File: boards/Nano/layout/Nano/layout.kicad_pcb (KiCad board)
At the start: 4 copper layers, 22 x 22 mm, 26 parts, among them U1 ?

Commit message: first pass
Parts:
- removed H1, H2, H3, H4: M2 DIN965 TopBottom, MountingHole_2.2mm_M2_DIN965_Pad_TopBottom:MountingHole_2.2mm_M2_DIN965_Pad_TopBottom
- removed R10: 1k, R_0402_1005Metric:R_0402_1005Metric
- removed R6, R7, R8, R9: 820, R_0402_1005Metric:R_0402_1005Metric
- removed U1: ?, InvenSense_QFN-24_3x3mm_P0.4mm:InvenSense_QFN-24_3x3mm_P0.4mm
- added C10: 100nF 10V, C_0402_1005Metric:C_0402_1005Metric, B.Cu at (80.5, 103.9)
- added C11: 100nF 6.3V, C_0402_1005Metric:C_0402_1005Metric, F.Cu at (85.4, 108.7)
- added C12: 100nF 10V, C_0402_1005Metric:C_0402_1005Metric, F.Cu at (83.1, 101.6)
- added C13: 100nF 10V, C_0402_1005Metric:C_0402_1005Metric, F.Cu at (87.6, 103.4)
- added C14: 100nF 10V, C_0402_1005Metric:C_0402_1005Metric, F.Cu at (87.6, 104.3)
- added C15: 4.7uF 10V, C_0603_1608Metric:C_0603_1608Metric, F.Cu at (88.2, 105.6)
- added IC1: ATMEGA328PMAU, QFP80P900X900X120-32N:QFP80P900X900X120-32N, F.Cu at (86.8, 120.3)
- added IC2: AMS1117M5_0, SOT229P700X180-4N:SOT229P700X180-4N, B.Cu at (84.7, 107.2)
- added IC3: FT231XQMR, QFN50P400X400X80-21N:QFN50P400X400X80-21N, F.Cu at (84.0, 105.1)
- added J1: 2.54mm 15x1, PinHeader_1x15_P2.54mm_Vertical:PinHeader_1x15_P2.54mm_Vertical, B.Cu at (75.1, 95.2)
- added J2: 2.54mm 15x1, PinHeader_1x15_P2.54mm_Vertical:PinHeader_1x15_P2.54mm_Vertical, B.Cu at (96.0, 95.2)
- added J3: 10118194M0001LF, 101181940001LF:101181940001LF, F.Cu at (85.3, 92.9)
- added J4: 2.54mm 3x2, PinHeader_2x03_P2.54mm_Vertical:PinHeader_2x03_P2.54mm_Vertical, F.Cu at (82.7, 134.4)
- added S1: SKRKAHE020, SKRKAEE020:SKRKAEE020, F.Cu at (79.3, 116.0)
- added Y1: 16MHz 18pF, Crystal_SMD_3225-4Pin_3.2x2.5mm:Crystal_SMD_3225-4Pin_3.2x2.5mm, F.Cu at (79.4, 123.7)
- C2, C3: value 100nF -> 100nF 6.3V
- C4: value 10nF -> 100nF 6.3V
- C5, C6: value 10nF -> 22pF C0G
- C7: value 10nF -> 10uF 25V; footprint C_0402_1005Metric:C_0402_1005Metric -> C_0805_2012Metric:C_0805_2012Metric; moved to B.Cu
- C8: value 10nF -> 100nF 25V; moved to B.Cu
- C9: value 100nF -> 22uF 10V; footprint C_0402_1005Metric:C_0402_1005Metric -> C_0805_2012Metric:C_0805_2012Metric; moved to B.Cu
- D1: value LED GREEN -> LED YELLOW; footprint LED_0402_1005Metric:LED_0402_1005Metric -> LED_0603_1608Metric:LED_0603_1608Metric
- D2: footprint LED_0402_1005Metric:LED_0402_1005Metric -> LED_0603_1608Metric:LED_0603_1608Metric
- R1: value 1k -> 10k 5%
- R2, R3: value 4.7k -> 1k 5%
- R4, R5: value 10k -> 27 5%
- moved C6 27.9 mm to (78.2, 125.9), turned to 180 degrees
- moved C3 24.1 mm to (80.6, 121.5), turned to 180 degrees
- moved C5 23.1 mm to (78.2, 121.5), turned to 180 degrees
- moved C4 20.4 mm to (93.0, 122.4), turned to 0 degrees
- moved C2 16.8 mm to (80.7, 120.0), turned to 180 degrees
- moved R1 12.5 mm to (86.5, 114.0), turned to 90 degrees
- moved D1 12.3 mm to (90.5, 111.7)
- moved C1 10.2 mm to (91.4, 107.6)
- moved R4 9.57 mm to (84.5, 108.7), turned to -90 degrees
- moved D2 8.58 mm to (91.0, 99.0)
- moved R5 8.36 mm to (83.5, 108.7)
- moved C7 8.33 mm to (86.4, 101.9)
- moved C8 7.32 mm to (88.7, 103.9), turned to 90 degrees
- moved R3 5.86 mm to (91.4, 105.6), turned to 0 degrees
- moved C9 4.80 mm to (82.9, 101.9), turned to 180 degrees
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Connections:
- C1 pad 1: vcc_VCC -> DTR
- C1 pad 2: gnd_GND -> RESET
- C2 pad 1: Imu.MPU9250.REGOUT -> VCC_5V
- C2 pad 2: gnd_GND -> GND
- C3 pad 1: vcc_VCC -> VCC_5V
- C3 pad 2: gnd_GND -> GND
- C4 pad 1: vcc_VCC -> VCC_5V
- C4 pad 2: gnd_GND -> GND
- C5 pad 1: LowPassFilter.STAGE1_OUT -> MCU.oscpair_XIN
- C5 pad 2: gnd_GND -> GND
- C6 pad 1: LowPassFilter.STAGE2_OUT -> MCU.oscpair_XOUT
- C6 pad 2: gnd_GND -> GND
- C7 pad 1: LowPassFilter.STAGE3_OUT -> USB_VBUS
- C7 pad 2: gnd_GND -> GND
- C8 pad 1: MCU_IN -> USB_VBUS
- C8 pad 2: gnd_GND -> GND
- C9 pad 1: vcc_VCC -> VCC_5V
- C9 pad 2: gnd_GND -> GND
- D1 pad 1: Imu.LED.L -> GND
- D1 pad 2: vcc_VCC -> LED_L_ANODE
- D2 pad 1: PowerLed.L -> GND
- D2 pad 2: vcc_VCC -> LED_PWR_ANODE
- R1 pad 1: Imu.LED.L -> RESET
- R1 pad 2: gnd_GND -> VCC_5V
- R2 pad 1: Imu.NC_2 -> D13
- R2 pad 2: vcc_VCC -> LED_L_ANODE
- R3 pad 1: Imu.NC -> VCC_5V
- R3 pad 2: vcc_VCC -> LED_PWR_ANODE
- R4 pad 1: Imu.MPU9250.CS_PULLUP -> USB_SERIAL.USBDM_INTERNAL
- R4 pad 2: vcc_VCC -> USB_DATA_D_N
- R5 pad 1: SENSOR_OUT -> USB_SERIAL.USBDP_INTERNAL
- R5 pad 2: vcc_VCC -> USB_DATA_D_P
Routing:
- net LowPassFilter.STAGE3_OUT: track 2.35 -> 0.00 mm
- net LowPassFilter.STAGE2_OUT: track 2.35 -> 0.00 mm
- net LowPassFilter.STAGE1_OUT: track 2.35 -> 0.00 mm
- net MCU_IN: track 1.34 -> 0.00 mm
- removed copper zone on B.Cu, net gnd_GND
- removed copper zone on F.Cu, net gnd_GND
- removed copper zone on In1.Cu, net gnd_GND
- removed copper zone on In2.Cu, net gnd_GND
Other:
- board size 22 x 22 mm -> 24.5 x 46.4 mm
- copper layers 4 -> 2
- board text removed: "0"
- board text removed: "0 mm"
- board text removed: "0.01 mm"
- board text removed: "0.02"
- board text removed: "0.035 mm"
- board text removed: "0.1 mm"
- board text removed: "1"
- board text removed: "1.24 mm"
- board text removed: "3.3"
- board text removed: "4.5"
- board text removed: "B.Cu"
- board text removed: "B.Mask"
- board text removed: "B.Paste"
- board text removed: "B.Silkscreen"
- board text removed: "Bottom Silk Screen"
- board text removed: "Bottom Solder Mask"
- board text removed: "Bottom Solder Paste"
- board text removed: "Color"
- board text removed: "DESIGN IN PROGRESS"
- board text removed: "Dielectric"
- board text removed: "Epsilon R"
- board text removed: "F.Cu"
- board text removed: "F.Mask"
- board text removed: "F.Paste"
- board text removed: "F.Silkscreen"
- board text removed: "FR4"
- board text removed: "In1.Cu"
- board text removed: "In2.Cu"
- board text removed: "Layer Name"
- board text removed: "Loss Tangent"
- board text removed: "Material"
- board text removed: "Not specified"
- board text removed: "PLACEHOLDER"
- board text removed: "Thickness (mm)"
- board text removed: "Top Silk Screen"
- board text removed: "Top Solder Mask"
- board text removed: "Top Solder Paste"
- board text removed: "Type"
- board text removed: "copper"
- board text removed: "core"
- board text removed: "prepreg"

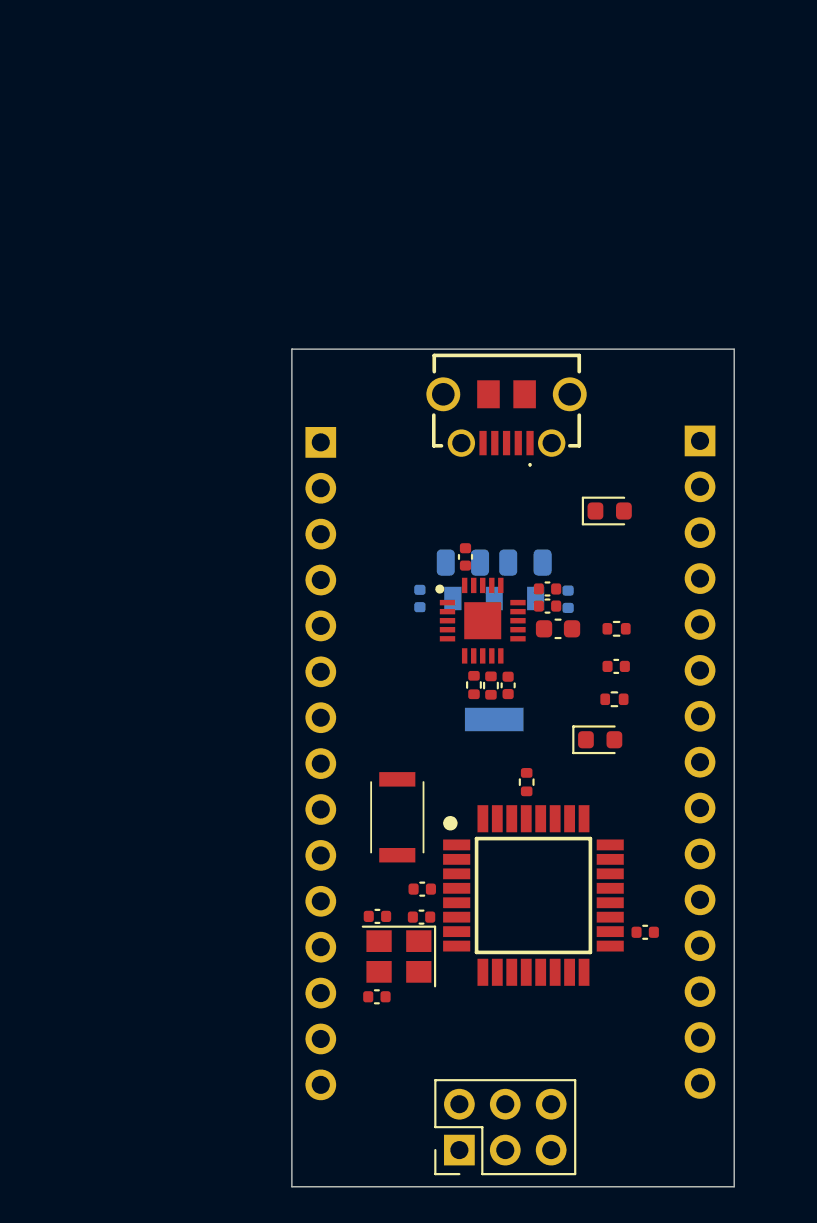
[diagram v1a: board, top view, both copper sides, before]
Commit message: blue solder mask
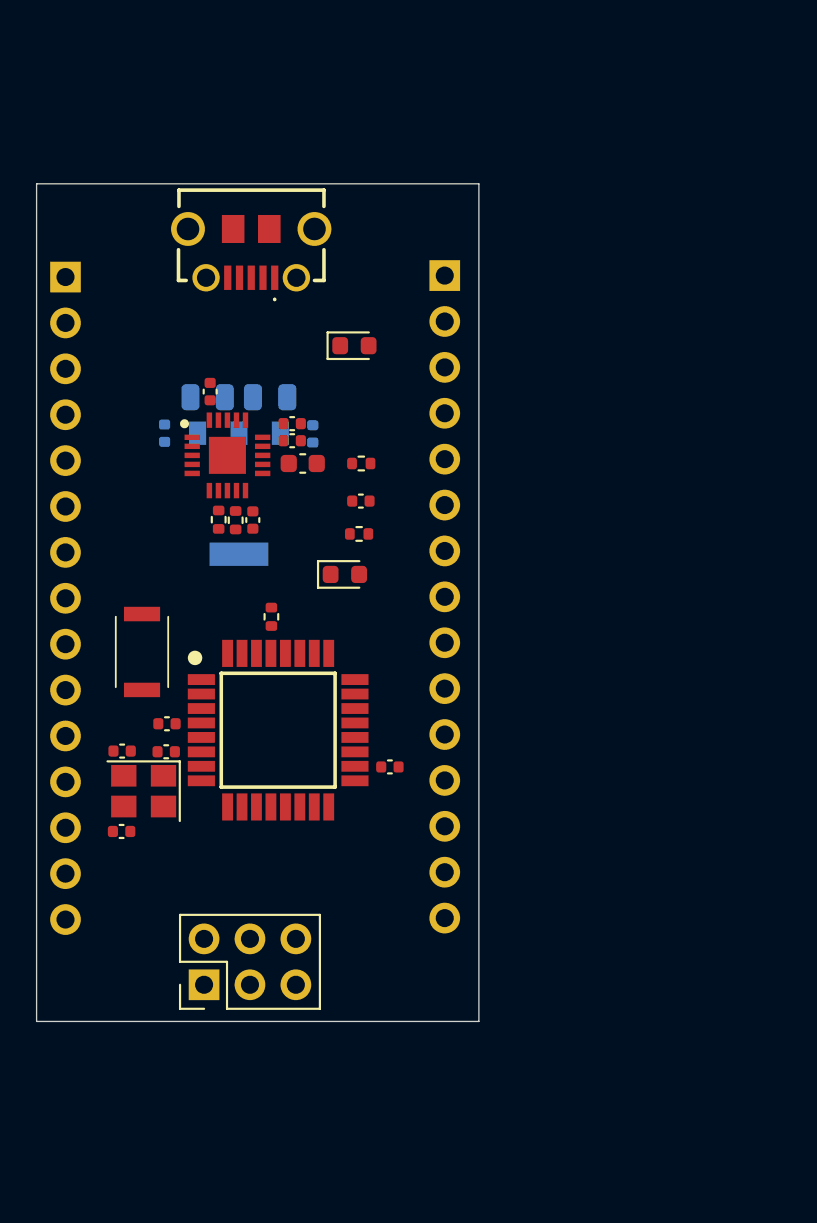
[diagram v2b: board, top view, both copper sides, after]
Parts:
- moved C3 16.8 mm to (66.5, 112.4)
- moved J3 16.8 mm to (71.2, 83.8)
- moved R3 16.8 mm to (77.3, 96.4)
- moved R4 16.8 mm to (70.3, 99.6)
- moved C6 16.8 mm to (64.0, 116.8)
- moved C9 16.8 mm to (68.8, 92.7)
- moved J4 16.8 mm to (68.6, 125.3)
- moved Y1 16.8 mm to (65.3, 114.5)
- moved C1 16.8 mm to (77.3, 98.5)
- moved C10 16.8 mm to (66.4, 94.7)
- moved C13 16.8 mm to (73.5, 94.2)
- moved C15 16.8 mm to (74.1, 96.4)
- moved C2 16.8 mm to (66.5, 110.8)
- moved C4 16.8 mm to (78.9, 113.2)
- moved C8 16.8 mm to (74.6, 94.8)
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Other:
- copper layers 2 -> 4
- board text added: "0"
- board text added: "0 mm"
- board text added: "0.01 mm"
- board text added: "0.0152 mm"
- board text added: "0.025"
- board text added: "0.035 mm"
- board text added: "0.0900 mm / 0.0900 mm"
- board text added: "0.1500 mm"
- board text added: "0.2104 mm"
- board text added: "1"
- board text added: "1.065 mm"
- board text added: "1.6000 mm"
- board text added: "24.4800 mm x 46.3600 mm"
- board text added: "3.3"
- board text added: "4"
- board text added: "4.4"
- board text added: "4.6"
- board text added: "B.Cu"
- board text added: "B.Mask"
- board text added: "B.Paste"
- board text added: "B.Silkscreen"
- board text added: "BOARD CHARACTERISTICS"
- board text added: "Blue"
- board text added: "Board Thickness:"
- board text added: "Board overall dimensions:"
- board text added: "Bottom Silk Screen"
- board text added: "Bottom Solder Mask"
- board text added: "Bottom Solder Paste"
- board text added: "Castellated pads:"
- board text added: "Color"
- board text added: "Copper Finish:"
- board text added: "Copper Layer Count:"
- board text added: "Dielectric"
- board text added: "ENIG"
- board text added: "Edge card connectors:"
- board text added: "Epsilon R"
- board text added: "F.Cu"
- board text added: "F.Mask"
- board text added: "F.Paste"
- board text added: "F.Silkscreen"
- board text added: "FR4-Core"
- board text added: "Impedance Control:"
- board text added: "In1.Cu"
- board text added: "In2.Cu"
- board text added: "Layer Name"
- board text added: "Loss Tangent"
- board text added: "Material"
- board text added: "Min hole diameter:"
- board text added: "Min track/spacing:"
- board text added: "No"
- board text added: "Not specified"
- board text added: "Plated Board Edge:"
- board text added: "Prepreg"
- board text added: "Thickness (mm)"
- board text added: "Top Silk Screen"
- board text added: "Top Solder Mask"
- board text added: "Top Solder Paste"
- board text added: "Type"
- board text added: "White"
- board text added: "copper"
- board text added: "core"
- board text added: "prepreg"

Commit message: better connector
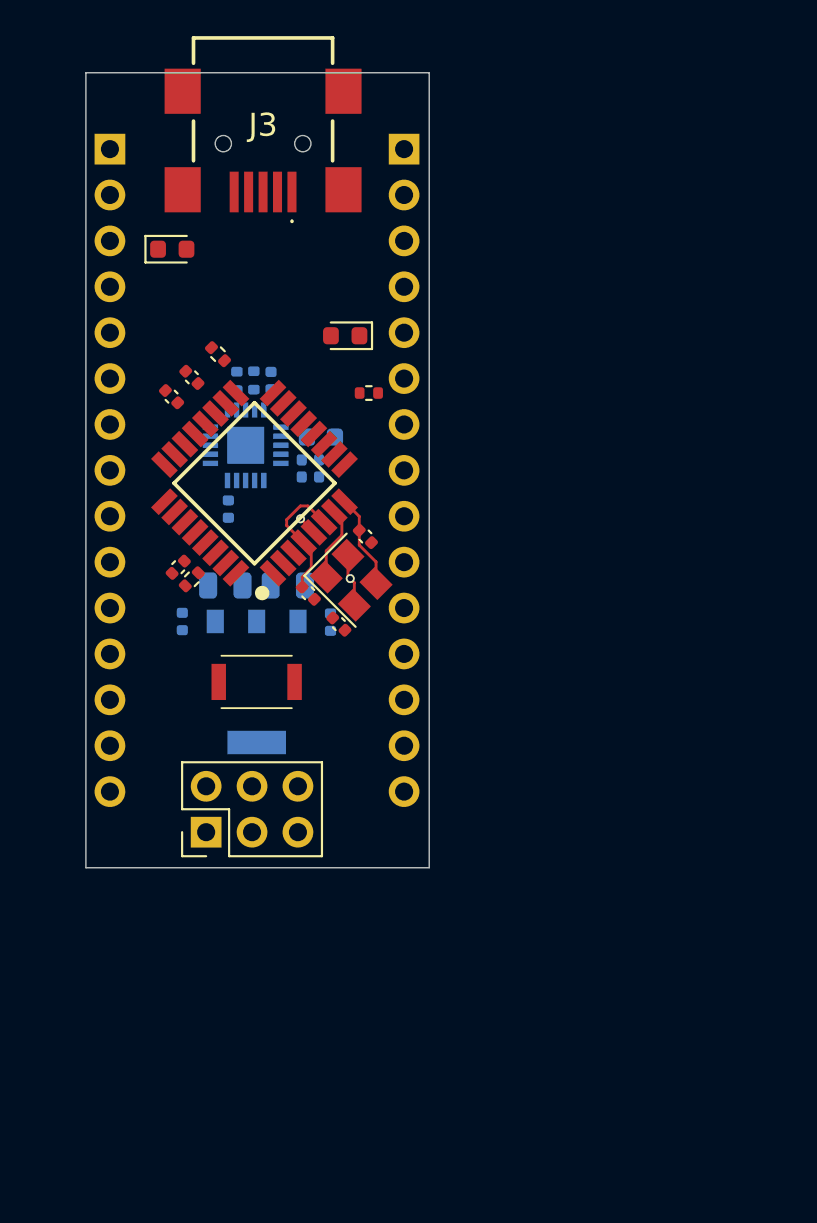
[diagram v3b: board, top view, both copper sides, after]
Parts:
- C11, C12, C13, C14, C15, IC3, R4, R5: moved to B.Cu
- J3: value 10118194M0001LF -> 10033526MN3212LF; footprint 101181940001LF:101181940001LF -> 10033526N3212LF:10033526N3212LF
- moved C6 21.2 mm to (77.5, 100.4), turned to -45 degrees
- moved D1 20.4 mm to (66.8, 84.5)
- moved C3 19.7 mm to (66.8, 92.7), turned to 135 degrees
- moved C2 19.2 mm to (67.9, 91.6), turned to 135 degrees
- moved Y1 16.4 mm to (76.7, 102.9), turned to -45 degrees
- moved C5 13.9 mm to (76.1, 105.3), turned to -45 degrees
- moved IC1 13.7 mm to (71.4, 97.5), turned to 135 degrees
- moved R2 12.6 mm to (69.4, 90.4), turned to 135 degrees
- moved C1 10.8 mm to (67.2, 102.2), turned to 45 degrees
- moved C4 10.6 mm to (74.4, 103.6), turned to -45 degrees
- moved C10 10.5 mm to (67.4, 105.2)
- moved IC2 10.5 mm to (71.5, 108.5)
- moved C8 10.5 mm to (75.6, 105.2)
- moved C7 10.5 mm to (73.2, 103.2)
- moved C9 10.5 mm to (69.8, 103.2)
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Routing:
- net VCC_5V: track 0.00 -> 7.26 mm
- net MCU.oscpair_XOUT: track 0.00 -> 5.24 mm
- net MCU.oscpair_XIN: track 0.00 -> 4.14 mm
- net GND: track 0.00 -> 3.96 mm, vias 0 -> 2
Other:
- board size 24.5 x 46.4 mm -> 19 x 44 mm

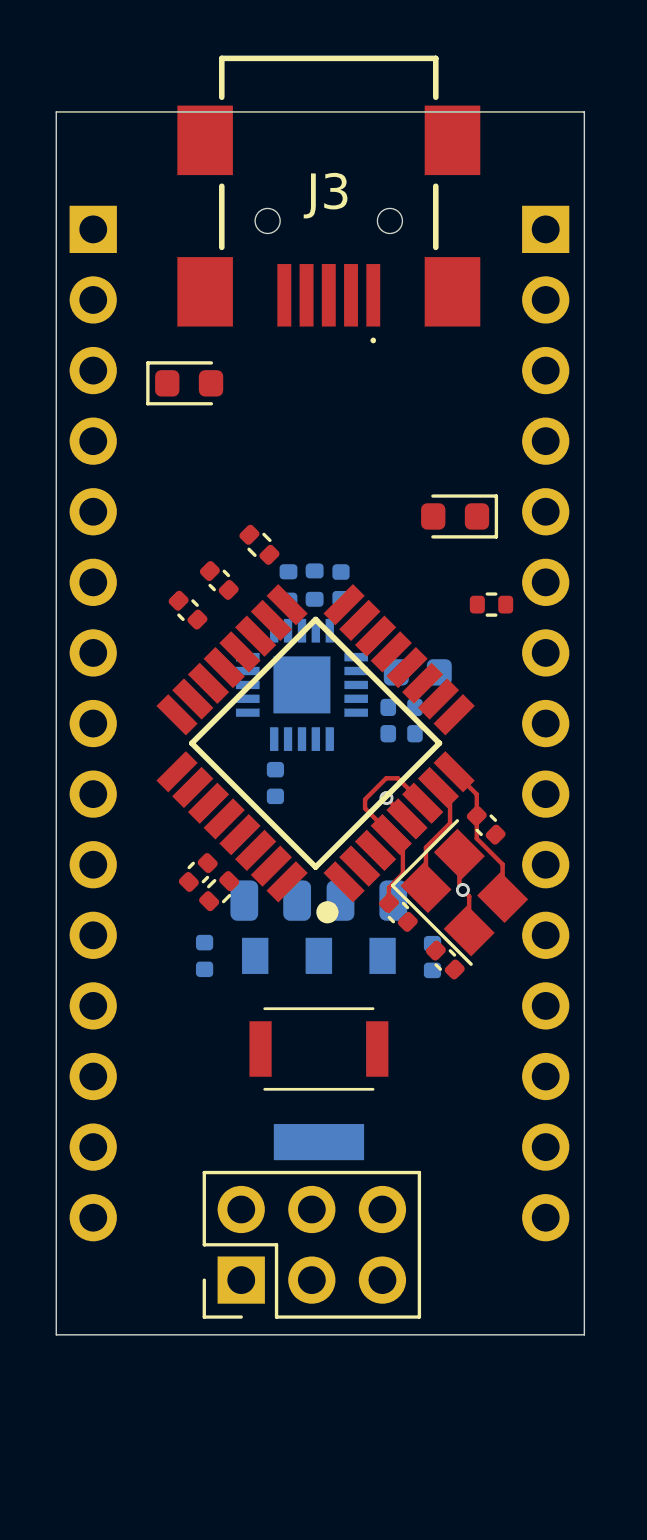
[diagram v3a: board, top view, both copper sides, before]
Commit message: add uart LEDs
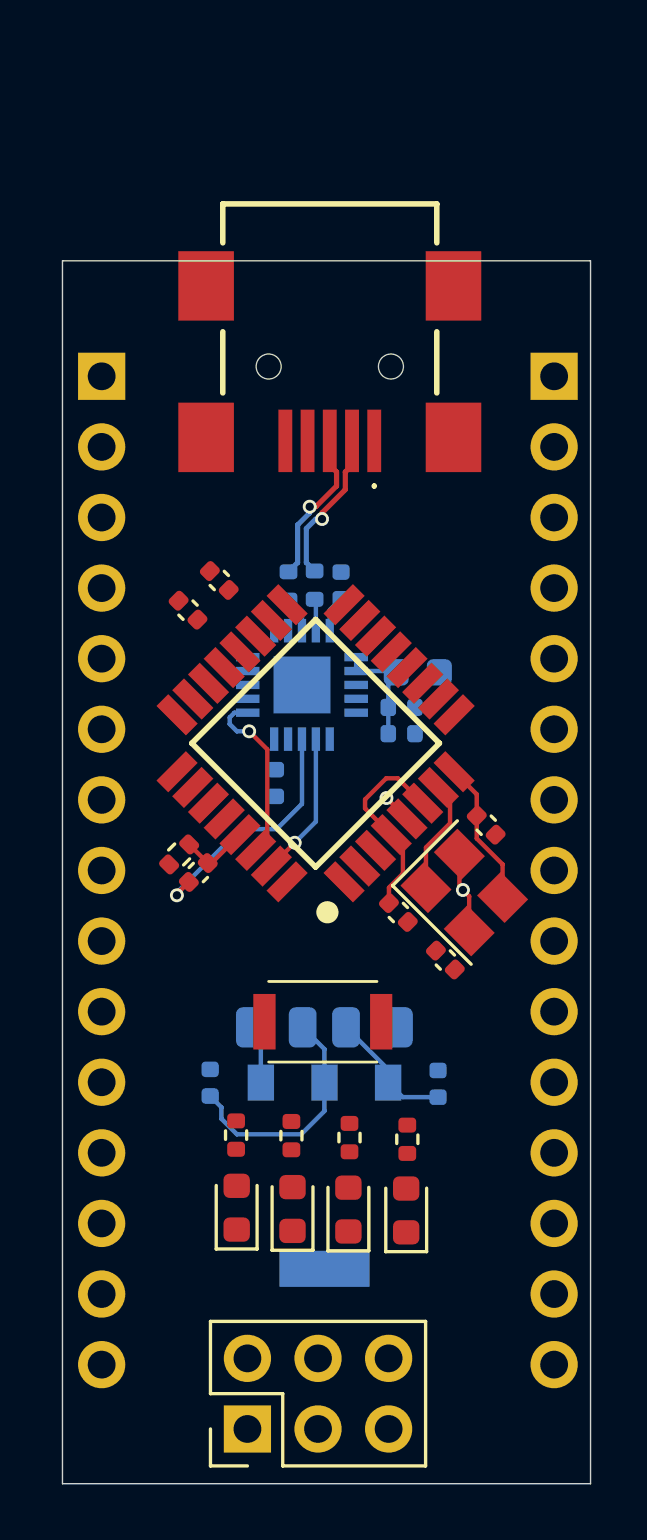
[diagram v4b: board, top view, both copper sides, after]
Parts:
- added D3: LED YELLOW, LED_0603_1608Metric:LED_0603_1608Metric, F.Cu at (72.6, 114.3)
- added D4: LED YELLOW, LED_0603_1608Metric:LED_0603_1608Metric, F.Cu at (74.7, 114.3)
- added R4: 1k 5%, R_0402_1005Metric:R_0402_1005Metric, F.Cu at (72.6, 111.7)
- added R5: 1k 5%, R_0402_1005Metric:R_0402_1005Metric, F.Cu at (74.7, 111.7)
- moved D1 29.7 mm to (68.6, 114.2), turned to 90 degrees
- moved D2 25.6 mm to (70.6, 114.3), turned to 90 degrees
- moved R2 21.3 mm to (68.5, 111.6), turned to -90 degrees
- moved R3 20.4 mm to (70.5, 111.6), turned to -90 degrees
- moved J4 5.36 mm to (68.9, 122.2)
- moved J1 5.29 mm to (63.7, 84.3)
- moved J2 5.29 mm to (80.0, 84.3)
- moved J3 5.24 mm to (71.9, 82.7)
- moved C8 4.56 mm to (75.8, 109.8)
- moved C9 4.56 mm to (70.0, 107.7)
- moved C10 4.56 mm to (67.6, 109.7)
- moved C7 4.56 mm to (73.4, 107.7)
- moved IC2 4.56 mm to (71.7, 113.1)
- moved R1 1.95 mm to (66.5, 101.5)
- moved S1 0.99 mm to (71.7, 107.5)
- renumbered R4 to R6, R5 to R7
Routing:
- net VCC_5V: track 7.26 -> 20.2 mm
- net DTR: track 0.00 -> 8.91 mm, vias 0 -> 1
- net UART_RX: track 0.00 -> 6.49 mm, vias 0 -> 1
- net USB_DATA_D_P: track 0.00 -> 5.66 mm, vias 0 -> 1
- net USB_DATA_D_N: track 0.00 -> 5.62 mm, vias 0 -> 1
- net UART_TX: track 0.00 -> 5.23 mm, vias 0 -> 1
- net USB_VBUS: track 0.00 -> 4.63 mm
- net RESET: track 0.00 -> 2.53 mm
- net GND: track 3.96 -> 6.11 mm
- net USB_SERIAL.P3V3OUT: track 0.00 -> 1.32 mm
- net USB_SERIAL.USBDP_INTERNAL: track 0.00 -> 1.30 mm
- net USB_SERIAL.USBDM_INTERNAL: track 0.00 -> 1.15 mm
